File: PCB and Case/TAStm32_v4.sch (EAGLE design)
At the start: 47 parts, among them IC1 74AVCH4T245PW,118, IC2 74AVCH4T245PW,118, IC3 74AVCH4T245PW,118, J1 ZX62D-B-5PA8, J10 RJSSE538002, J11 RJSSE538002, J12 SOICBITE, J13 CONSOLE_RESET, J2 UE27-AC54-100, J3 TSM-105-02-L-SHJ, J4 CONSOLE_RESET, J5 OLED128X64, J6 SAMTEC-TSM-116-01-X-SVJ, J7 SAMTEC-TSM-116-01-X-SVJ, U1 STM32F446RET6, U2 3.3V REG, Y1 8MHz

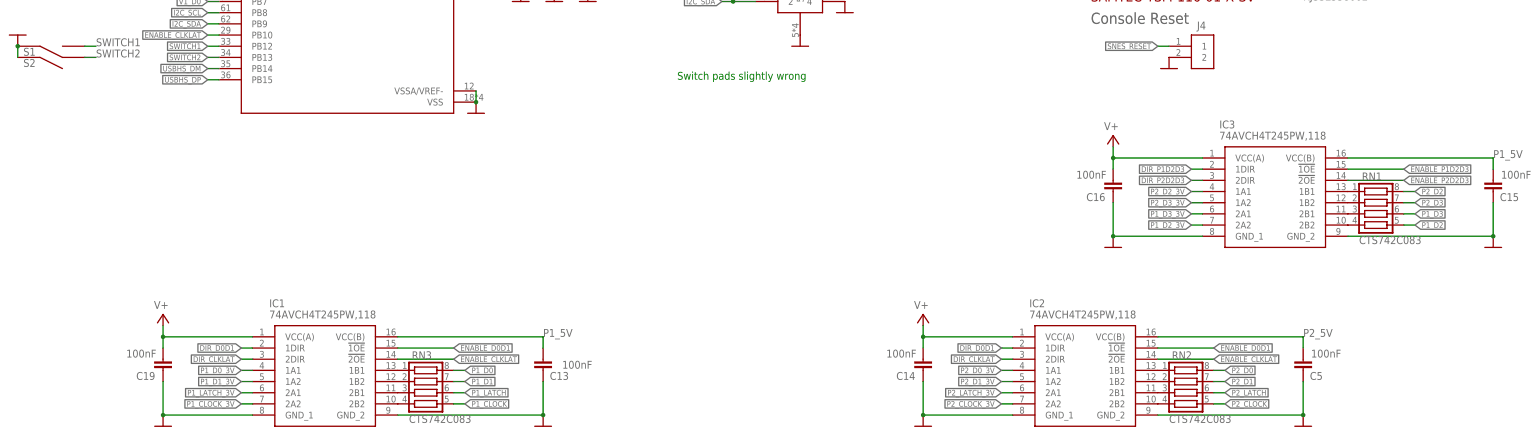
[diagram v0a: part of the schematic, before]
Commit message: Pin reshuffle for proto
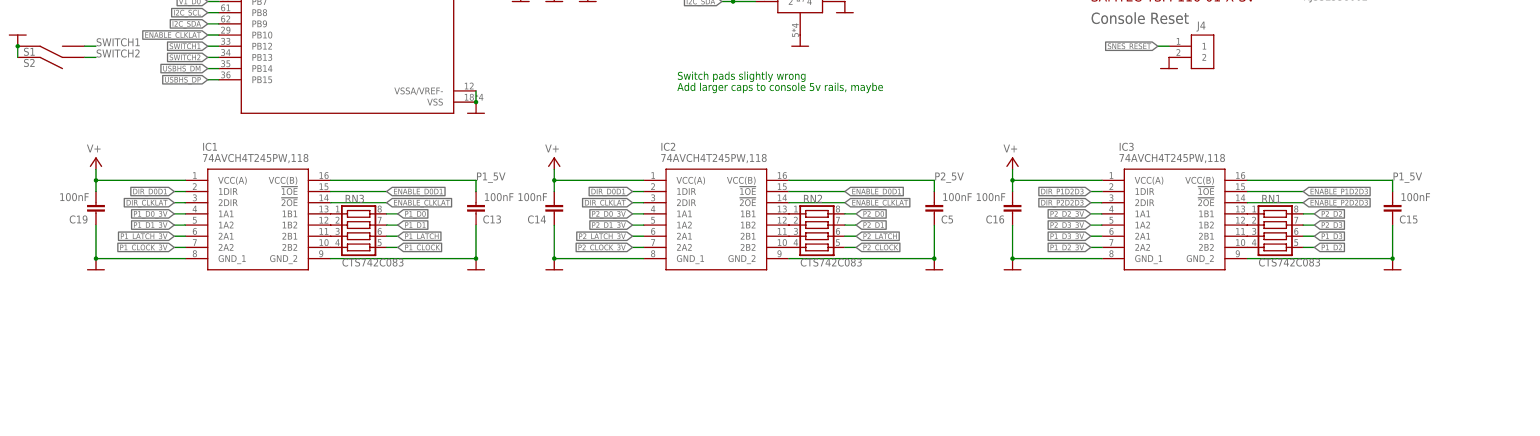
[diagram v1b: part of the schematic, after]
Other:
- note added: "Add larger caps to console 5v rails, maybe"
- moved on the sheet: C13, C14, C15, C16, C19, C5, IC1, IC2, IC3, RN1, RN2, RN3

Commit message: notes
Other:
- note added: "Add insurance caps to outputs (maybe arrays)"
- note added: "Label debug pins"
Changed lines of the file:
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@@
 <text x="-17.78" y="-58.42" size="1.778" layer="91">Switch pads slightly wrong</text>
 <text x="-17.78" y="-60.96" size="1.778" layer="91">Add larger caps to console 5v rails, maybe</text>
+<text x="-17.78" y="-63.5" size="1.778" layer="91">Add insurance caps to outputs (maybe arrays)</text>
+<text x="-17.78" y="-66.04" size="1.778" layer="91">Label debug pins</text>
 </plain>
 <instances>

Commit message: more new buffers
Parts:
- removed C15, C16, C19: 100nF, rcl:C-EUC0603K
- removed IC1, IC2, IC3: 74AVCH4T245PW,118, SamacSys_Parts:74AVCH4T245PW,118
- removed RN3: CTS742C083, resistor-net:CTS742C083
- added IC4: 74LVC14, 74xx-us:74LS14D
- added IC5: 74HCT125, 74xx-eu:74ABT125PW
- added IC7: 74LVC07, 74xx-us:74LS07D
- added RN4, RN5: CTS742C083, resistor-net:CTS742C083
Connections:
- removed net N$10: IC2.2B2, RN2.4
- removed net N$11: IC2.1B1, RN2.1
- removed net N$12: IC1.1B2, RN3.2
- removed net N$13: IC1.2B1, RN3.3
- removed net N$14: IC1.2B2, RN3.4
- removed net N$15: IC1.1B1, RN3.1
- removed net N$4: IC3.2B1, RN1.3
- removed net N$6: IC3.2B2, RN1.4
- removed net N$8: IC2.1B2, RN2.2
- removed net N$9: IC2.2B1, RN2.3
- removed net P1_5V: C13.2, C15.2, D1.A, IC1.VCC(B), IC3.VCC(B), J10.L2, J6.10
- removed net P2_5V: C5.2, D2.A, IC2.VCC(B), J10.R2, J6.2
- new net GND1: C13.1
- new net N$16: IC4A.I, RN1.1, RN4.8
- new net N$17: IC4B.I, RN1.2, RN4.7
- new net N$18: IC4C.I, RN1.3, RN4.6
- new net N$21: IC4F.I, RN2.3, RN5.6
- new net OUTPUTS_ENABLE: IC5A.OE, IC5B.OE, IC5C.OE, IC5D.OE
- new net P1_D2_3V_IN: IC4C.O
- new net P1_VCC: D1.A, J10.L2, J6.10
- new net P2_D3_3V_IN: IC4F.O
- new net P2_VCC: D2.A, J10.R2, J6.2
- new net V+1: C14.2, IC5P.VCC
- net DIR_CLKLAT: no longer IC1.2DIR, IC2.2DIR
- net DIR_D0D1: no longer IC1.1DIR, IC2.1DIR
- net DIR_P1D2D3: no longer IC3.1DIR
- net DIR_P2D2D3: no longer IC3.2DIR
- net ENABLE_CLKLAT: no longer IC1.!2OE, IC2.!2OE
- net ENABLE_D0D1: no longer IC1.!1OE, IC2.!1OE
- net ENABLE_P1D2D3: no longer IC3.!1OE
- net ENABLE_P2D2D3: no longer IC3.!2OE
- net GND: now also IC4P.GND, IC5P.GND, IC7E.I, IC7F.I, IC7P.GND; no longer C13.1, C15.1, C16.1, C19.1, IC1.GND_1, IC1.GND_2, IC2.GND_1, IC2.GND_2, IC3.GND_1, IC3.GND_2
- net N$2: now also IC4D.I, RN2.1, RN5.8; no longer IC3.1B1, RN1.1
- net N$3: now also IC4E.I, RN2.2, RN5.7; no longer IC3.1B2, RN1.2
- net P1_CLOCK: now also RN4.2; no longer RN3.5
- net P1_CLOCK_3V: now also IC4B.O; no longer IC1.2A2
- net P1_D0: now also IC5A.O; no longer RN3.8
- net P1_D0_3V: now also IC5A.I; no longer IC1.1A1
- net P1_D1: now also IC5B.O; no longer RN3.7
- net P1_D1_3V: now also IC5B.I; no longer IC1.1A2
- net P1_D2: now also IC7A.O, RN4.3; no longer RN1.5
- net P1_D2_3V: now also IC7A.I; no longer IC3.2A2
- net P1_D3: now also IC7B.O; no longer RN1.6
- net P1_D3_3V: now also IC7B.I; no longer IC3.2A1
- net P1_LATCH: now also RN4.1; no longer RN3.6
- net P1_LATCH_3V: now also IC4A.O; no longer IC1.2A1
- net P2_CLOCK: now also RN5.2; no longer RN2.5
- net P2_CLOCK_3V: now also IC4E.O; no longer IC2.2A2
- net P2_D0: now also IC5C.O; no longer RN2.8
- net P2_D0_3V: now also IC5C.I; no longer IC2.1A1
- net P2_D1: now also IC5D.O; no longer RN2.7
- net P2_D1_3V: now also IC5D.I; no longer IC2.1A2
- net P2_D2: now also IC7C.O; no longer RN1.8
- net P2_D2_3V: now also IC7C.I; no longer IC3.1A1
- net P2_D3: now also IC7D.O, RN5.3; no longer RN1.7
- net P2_D3_3V: now also IC7D.I; no longer IC3.1A2
- net P2_LATCH: now also RN5.1; no longer RN2.6
- net P2_LATCH_3V: now also IC4D.O; no longer IC2.2A1
- net V+: now also C13.2, C5.2, IC4P.VCC, IC7P.VCC, RN1.6, RN1.7, RN1.8, RN2.6, RN2.7, RN2.8; no longer C14.2, C16.2, C19.2, IC1.VCC(A), IC2.VCC(A), IC3.VCC(A)
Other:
- moved on the sheet: C13, C14, C5, RN1, RN2

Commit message: bleh updates
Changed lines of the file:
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@@
 <wire x1="-45.72" y1="-109.22" x2="-45.72" y2="-121.92" width="0.1524" layer="91"/>
 <wire x1="-45.72" y1="-121.92" x2="-40.64" y2="-121.92" width="0.1524" layer="91"/>
+<junction x="-45.72" y="-121.92"/>
 </segment>
 </net>
@@
 <net name="OUTPUTS_ENABLE" class="0">
 <segment>
-<label x="10.16" y="-109.22" size="1.27" layer="95" rot="R180" xref="yes"/>
+<label x="20.32" y="-109.22" size="1.27" layer="95" rot="R180" xref="yes"/>
 <pinref part="IC5" gate="D" pin="OE"/>
 <pinref part="IC5" gate="C" pin="OE"/>
@@
 <junction x="66.04" y="-109.22"/>
 <junction x="22.86" y="-109.22"/>
-<wire x1="22.86" y1="-109.22" x2="10.16" y2="-109.22" width="0.1524" layer="91"/>
+<wire x1="22.86" y1="-109.22" x2="20.32" y2="-109.22" width="0.1524" layer="91"/>
 </segment>
 </net>

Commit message: more code work
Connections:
- net P2_D3_3V_IN renamed P2_D2_3V_IN
- net OUTPUTS_ENABLE: now also RN2.4
- net V+: now also RN2.5
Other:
- moved on the sheet: RN1
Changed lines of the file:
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@@
 <part name="SUPPLY17" library="supply2" library_urn="urn:adsk.eagle:library:372" deviceset="V+" device=""/>
 <part name="SUPPLY18" library="supply2" library_urn="urn:adsk.eagle:library:372" deviceset="V+" device=""/>
+<part name="SUPPLY19" library="supply2" library_urn="urn:adsk.eagle:library:372" deviceset="V+" device=""/>
 </parts>
 <sheets>
@@
 <attribute name="VALUE" x="91.059" y="-112.776" size="1.778" layer="96" rot="R90"/>
 </instance>
-<instance part="RN1" gate="G$1" x="-129.54" y="-109.22" smashed="yes" rot="R90">
-<attribute name="NAME" x="-134.62" y="-111.125" size="1.778" layer="95" rot="R90"/>
-<attribute name="VALUE" x="-120.142" y="-116.84" size="1.778" layer="96" rot="R90"/>
-</instance>
-<instance part="SUPPLY10" gate="1" x="-132.08" y="-99.06" smashed="yes" rot="MR0">
-<attribute name="VALUE" x="-130.81" y="-97.79" size="1.778" layer="96" rot="MR0"/>
-</instance>
-<instance part="SUPPLY11" gate="1" x="-129.54" y="-99.06" smashed="yes" rot="MR0">
-<attribute name="VALUE" x="-128.27" y="-97.79" size="1.778" layer="96" rot="MR0"/>
-</instance>
-<instance part="SUPPLY15" gate="1" x="-127" y="-99.06" smashed="yes" rot="MR0">
-<attribute name="VALUE" x="-125.73" y="-97.79" size="1.778" layer="96" rot="MR0"/>
+<instance part="RN1" gate="G$1" x="-129.54" y="-104.14" smashed="yes" rot="R90">
+<attribute name="NAME" x="-134.62" y="-106.045" size="1.778" layer="95" rot="R90"/>
+<attribute name="VALUE" x="-120.142" y="-106.68" size="1.778" layer="96" rot="R90"/>
+</instance>
+<instance part="SUPPLY10" gate="1" x="-132.08" y="-93.98" smashed="yes" rot="MR0">
+<attribute name="VALUE" x="-130.81" y="-92.71" size="1.778" layer="96" rot="MR0"/>
+</instance>
+<instance part="SUPPLY11" gate="1" x="-129.54" y="-93.98" smashed="yes" rot="MR0">
+<attribute name="VALUE" x="-128.27" y="-92.71" size="1.778" layer="96" rot="MR0"/>
+</instance>
+<instance part="SUPPLY15" gate="1" x="-127" y="-93.98" smashed="yes" rot="MR0">
+<attribute name="VALUE" x="-125.73" y="-92.71" size="1.778" layer="96" rot="MR0"/>
 </instance>
 <instance part="RN2" gate="G$1" x="-48.26" y="-104.14" smashed="yes" rot="R90">
 <attribute name="NAME" x="-53.34" y="-106.045" size="1.778" layer="95" rot="R90"/>
-<attribute name="VALUE" x="-28.702" y="-111.76" size="1.778" layer="96" rot="R90"/>
+<attribute name="VALUE" x="-38.862" y="-106.68" size="1.778" layer="96" rot="R90"/>
 </instance>
 <instance part="SUPPLY16" gate="1" x="-50.8" y="-93.98" smashed="yes" rot="MR0">
@@
 <instance part="SUPPLY18" gate="1" x="-45.72" y="-93.98" smashed="yes" rot="MR0">
 <attribute name="VALUE" x="-44.45" y="-92.71" size="1.778" layer="96" rot="MR0"/>
+</instance>
+<instance part="SUPPLY19" gate="1" x="-43.18" y="-93.98" smashed="yes" rot="MR0">
+<attribute name="VALUE" x="-41.91" y="-92.71" size="1.778" layer="96" rot="MR0"/>
 </instance>
 </instances>
@@
 <pinref part="SUPPLY18" gate="1" pin="V+"/>
 </segment>
+<segment>
+<pinref part="RN2" gate="G$1" pin="5"/>
+<pinref part="SUPPLY19" gate="1" pin="V+"/>
+</segment>
 </net>
 <net name="I2C_SCL" class="0">
@@
 <pinref part="RN1" gate="G$1" pin="1"/>
 <wire x1="-132.08" y1="-116.84" x2="-116.84" y2="-116.84" width="0.1524" layer="91"/>
-<wire x1="-132.08" y1="-114.3" x2="-132.08" y2="-116.84" width="0.1524" layer="91"/>
+<wire x1="-132.08" y1="-109.22" x2="-132.08" y2="-116.84" width="0.1524" layer="91"/>
 <junction x="-132.08" y="-116.84"/>
 </segment>
@@
 <wire x1="-116.84" y1="-119.38" x2="-116.84" y2="-127" width="0.1524" layer="91"/>
 <pinref part="RN1" gate="G$1" pin="2"/>
-<wire x1="-129.54" y1="-114.3" x2="-129.54" y2="-119.38" width="0.1524" layer="91"/>
+<wire x1="-129.54" y1="-109.22" x2="-129.54" y2="-119.38" width="0.1524" layer="91"/>
 <junction x="-129.54" y="-119.38"/>
 </segment>
@@
 <wire x1="-119.38" y1="-137.16" x2="-116.84" y2="-137.16" width="0.1524" layer="91"/>
 <pinref part="RN1" gate="G$1" pin="3"/>
-<wire x1="-127" y1="-114.3" x2="-127" y2="-121.92" width="0.1524" layer="91"/>
+<wire x1="-127" y1="-109.22" x2="-127" y2="-121.92" width="0.1524" layer="91"/>
 <junction x="-127" y="-121.92"/>
 </segment>
@@
 </segment>
 </net>
-<net name="P2_D3_3V_IN" class="0">
+<net name="P2_D2_3V_IN" class="0">
 <segment>
 <wire x1="-17.78" y1="-137.16" x2="-15.24" y2="-137.16" width="0.1524" layer="91"/>
@@
 <net name="OUTPUTS_ENABLE" class="0">
 <segment>
-<label x="20.32" y="-109.22" size="1.27" layer="95" rot="R180" xref="yes"/>
+<label x="22.86" y="-109.22" size="1.27" layer="95" rot="R90" xref="yes"/>
 <pinref part="IC5" gate="D" pin="OE"/>
 <pinref part="IC5" gate="C" pin="OE"/>
@@
 <junction x="66.04" y="-109.22"/>
 <junction x="22.86" y="-109.22"/>
-<wire x1="22.86" y1="-109.22" x2="20.32" y2="-109.22" width="0.1524" layer="91"/>
-</segment>
-</net>
+<pinref part="RN2" gate="G$1" pin="4"/>
+<wire x1="22.86" y1="-109.22" x2="-43.18" y2="-109.22" width="0.1524" layer="91"/>
+</segment>
+</net>

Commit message: caps
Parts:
- added CN1, CN2: CA0612KRX7R7BB104, SamacSys_Parts:CA0612KRX7R7BB104
- added RN3: CTS742C083, resistor-net:CTS742C083
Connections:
- removed net N$21: IC4F.I, RN2.3, RN5.6
- new net N$4: CN2.8, IC4D.I, RN2.1, RN5.8
- new net N$6: CN2.7, IC4E.I, RN2.2, RN5.7
- new net N$8: CN2.6, IC4F.I, RN2.3, RN5.6
- net GND: now also CN1.1, CN1.2, CN1.3, CN1.4, CN2.1, CN2.2, CN2.3, CN2.4
- net N$16: now also CN1.8
- net N$17: now also CN1.7
- net N$18: now also CN1.6
- net N$2: now also IC5B.O, RN3.2; no longer IC4D.I, RN2.1, RN5.8
- net N$3: now also IC5A.O, RN3.1; no longer IC4E.I, RN2.2, RN5.7
- net P1_D0: now also RN3.8; no longer IC5A.O
- net P1_D1: now also RN3.7; no longer IC5B.O
- net P1_D2: now also RN3.6; no longer IC7A.O
- net P1_D3: now also RN3.5; no longer IC7B.O
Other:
- moved on the sheet: C13, C14, C5, IC4A, IC4B, IC4C, IC4P, IC5C, IC5D, IC5P, IC7A, IC7B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

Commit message: new new new new buffers
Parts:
- removed IC5: 74HCT125, 74xx-eu:74ABT125PW
- removed IC7: 74LVC07, 74xx-us:74LS07D
- added C15, C16, C17: 100nF, rcl:C-EUC0603K
- added CN3, CN4: CA0612KRX7R7BB104, SamacSys_Parts:CA0612KRX7R7BB104
- added IC1, IC2: 74HCT3G07DP-Q100H, SamacSys_Parts:74HCT3G07DP-Q100H
- added IC3: 74AVCH4T245PW,118, SamacSys_Parts:74AVCH4T245PW,118
- added RN7: CTS742C083, resistor-net:CTS742C083
- IC4: value 74LVC14 -> 74AVCH4T245PW,118; device 74xx-us:74LS14D -> SamacSys_Parts:74AVCH4T245PW,118
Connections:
- removed net DIR_CLKLAT: U1.PA0
- removed net ENABLE_CLKLAT: U1.PB10
- removed net GND1: C13.1
- removed net OUTPUTS_ENABLE: IC5A.OE, IC5B.OE, IC5C.OE, IC5D.OE, RN2.4
- removed net P1_D2_3V: IC7A.I, U1.PC4
- removed net P2_D2_3V: IC7C.I, U1.PC9
- removed net V+1: C14.2, IC5P.VCC
- new net N$10: IC3.2B2, RN3.4
- new net N$11: IC4.1B2, RN7.2
- new net N$12: IC4.1B1, RN7.1
- new net N$13: IC4.2B1, RN7.3
- new net N$14: IC4.2B2, RN7.4
- new net N$9: IC3.2B1, RN3.3
- new net P1_D2_3V_OUT: IC3.1A1, U1.PA1
- new net P2_D2_3V_OUT: IC4.2A1
- net DIR_D0D1: now also IC3.2DIR, IC4.1DIR, U1.PA2; no longer U1.PA1
- net DIR_P1D2D3: now also IC3.1DIR, U1.PA4; no longer U1.PB1
- net DIR_P2D2D3: now also IC4.2DIR
- net ENABLE_D0D1: now also IC3.!2OE, IC4.!1OE, U1.PA5; no longer U1.PA2
- net ENABLE_P1D2D3: now also IC3.!1OE, U1.PA6; no longer U1.PA5
- net ENABLE_P2D2D3: now also IC4.!2OE; no longer U1.PA4
- net GND: now also C13.2, C15.2, C16.1, C17.2, C5.2, CN3.1, CN3.2, CN3.3, CN3.4, CN4.1, CN4.2, CN4.3, CN4.4, IC1.GND, IC2.GND, IC3.GND_1, IC3.GND_2, IC4.GND_1, IC4.GND_2; no longer C5.1, IC4P.GND, IC5P.GND, IC7E.I, IC7F.I, IC7P.GND
- net N$16: now also IC1.1A; no longer IC4A.I
- net N$17: now also IC1.3A; no longer IC4B.I
- net N$18: now also IC1.2A; no longer IC4C.I
- net N$2: now also IC3.1B2; no longer IC5B.O
- net N$3: now also IC3.1B1; no longer IC5A.O
- net N$4: now also IC2.1A; no longer IC4D.I
- net N$6: now also IC2.3A; no longer IC4E.I
- net N$8: now also IC2.2A; no longer IC4F.I
- net P1_CLOCK_3V: now also IC1.3Y; no longer IC4B.O
- net P1_D0: now also CN3.8
- net P1_D0_3V: now also IC3.2A1; no longer IC5A.I
- net P1_D1: now also CN3.5
- net P1_D1_3V: now also IC3.2A2; no longer IC5B.I
- net P1_D2_3V_IN: now also IC1.2Y, U1.PC4; no longer IC4C.O
- net P1_D3_3V: now also IC3.1A2, U1.PA0; no longer IC7B.I
- net P1_LATCH_3V: now also IC1.1Y; no longer IC4A.O
- net P1_VCC: now also C15.1, C17.1, IC3.VCC(B), IC4.VCC(B)
- net P2_CLOCK_3V: now also IC2.3Y; no longer IC4E.O
- net P2_D0: now also CN4.5, RN7.7; no longer IC5C.O
- net P2_D0_3V: now also IC4.1A2; no longer IC5C.I
- net P2_D1: now also CN4.8, RN7.8; no longer IC5D.O
- net P2_D1_3V: now also IC4.1A1; no longer IC5D.I
- net P2_D2: now also RN5.3, RN7.6; no longer IC7C.O
- net P2_D2_3V_IN: now also IC2.2Y, U1.PC9; no longer IC4F.O
- net P2_D3: now also RN7.5; no longer IC7D.O, RN5.3
- net P2_D3_3V: now also IC4.2A2, U1.PB1; no longer IC7D.I, U1.PA6
- net P2_LATCH_3V: now also IC2.1Y; no longer IC4D.O
- net V+: now also C13.1, C14.2, C16.2, C5.1, IC1.VCC, IC2.VCC, IC3.VCC(A), IC4.VCC(A); no longer C13.2, C5.2, IC4P.VCC, IC7P.VCC
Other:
- note added: "make D2 able to be read from schmitt-triggered inputs (NES/SNES) or voltage translators (N64)"
- note added: "maybe omit pullups?"
- moved on the sheet: C13, C14, C5, RN1, RN2, RN3, RN4

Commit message: new buffer funtimes
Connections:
- net N$16: now also RN1.3; no longer RN1.1
- net N$17: now also RN1.1; no longer RN1.2
- net N$18: now also RN1.2; no longer RN1.3
- net N$4: now also CN2.6, RN2.2, RN5.6; no longer CN2.8, RN2.1, RN5.8
- net N$6: now also CN2.5, RN2.1, RN5.5; no longer CN2.7, RN2.2, RN5.7
- net N$8: now also CN2.8, RN2.4, RN5.8; no longer CN2.6, RN2.3, RN5.6
- net P1_D0: now also CN3.7, RN3.6; no longer CN3.8, RN3.8
- net P1_D1: now also CN3.8, RN3.5; no longer CN3.5, RN3.7
- net P1_D2: now also RN3.8; no longer RN3.6
- net P1_D3: now also RN3.7; no longer RN3.5
- net P1_D3_3V: no longer U1.PA7
- net P1_VCC: no longer C17.1, IC4.VCC(B)
- net P2_D0: now also CN4.8; no longer CN4.5
- net P2_D1: now also CN4.5; no longer CN4.8
- net P2_VCC: now also C17.1, IC4.VCC(B)
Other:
- note added: "Debug# ports"
- note removed: "Debug/expansion ports"
- moved on the sheet: C1, C10, C11, C12, C13, C14, C15, C16, C17, C2, C3, C4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
